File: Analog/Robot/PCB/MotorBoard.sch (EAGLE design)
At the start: 12 parts, among them U1 MSP430G2X53_20P

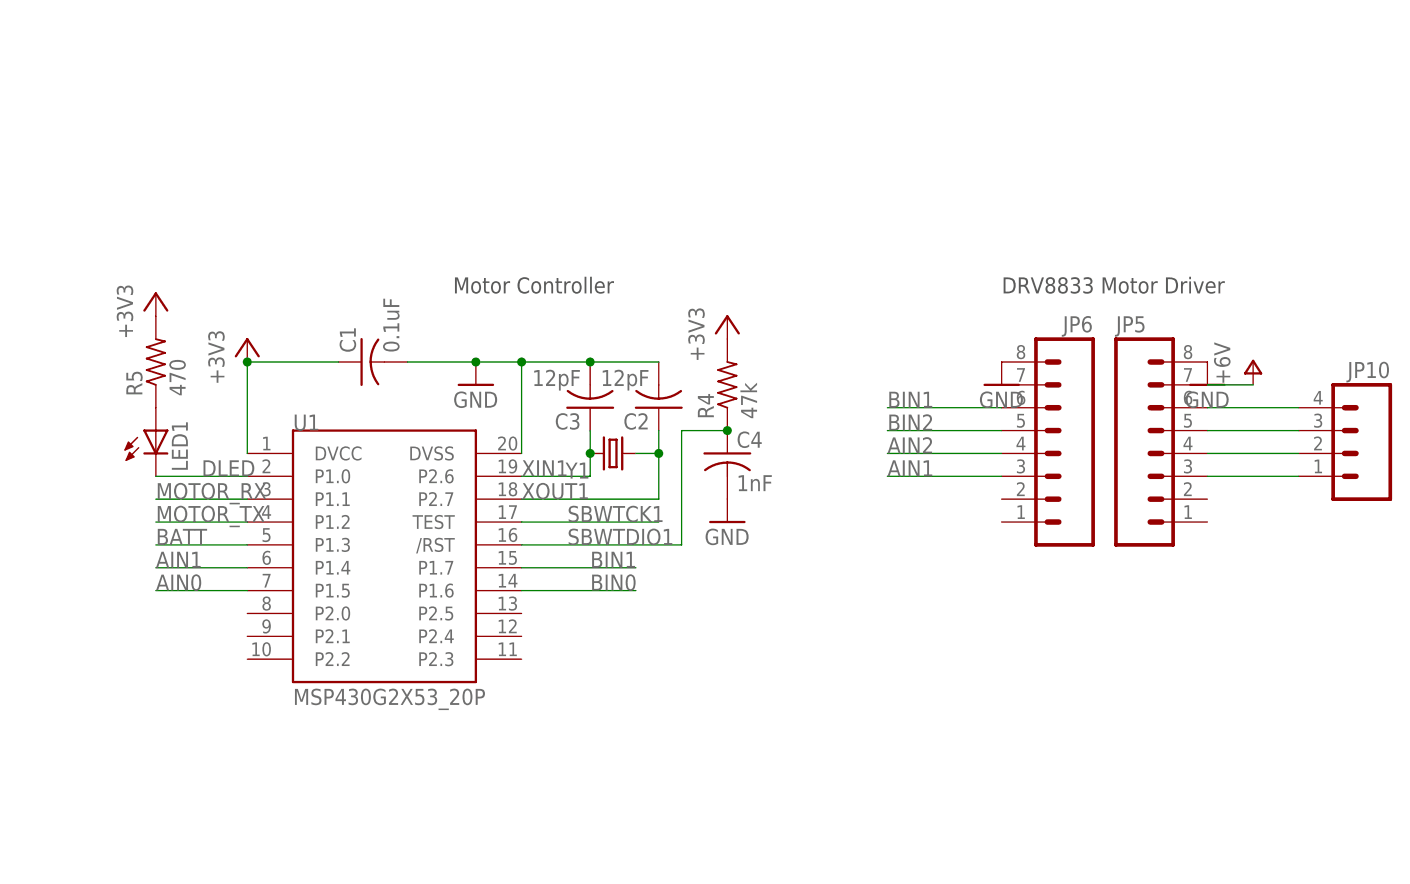
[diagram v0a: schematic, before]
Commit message: Board final; SPI progress
Sent PCBs to FAB
SPI driver working for multi-byte.  Bug: bytes are sent in reversed
order, although bit ordering (MSB first) is correct.
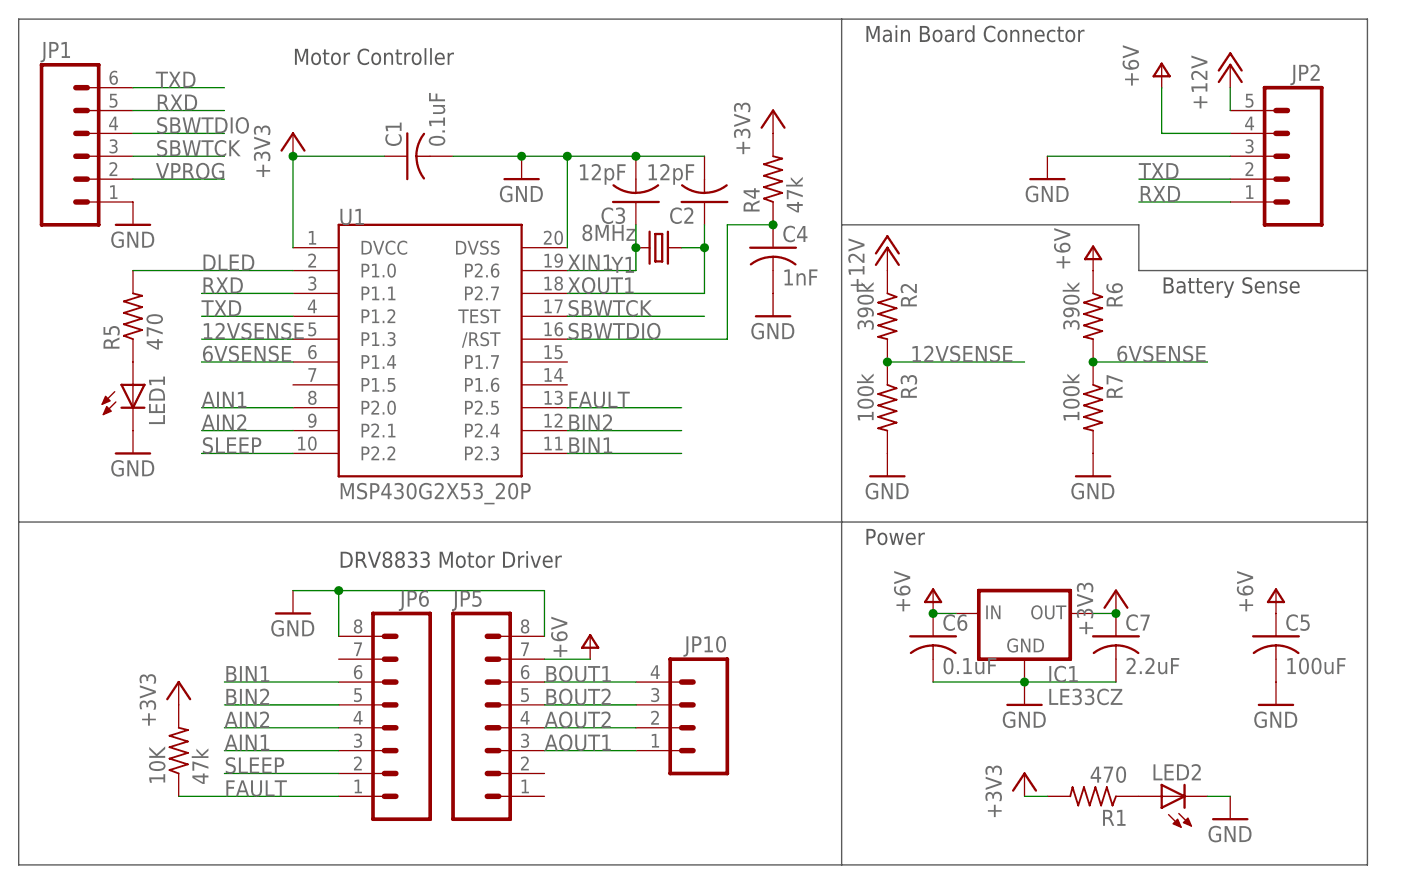
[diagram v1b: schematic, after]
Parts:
- added 10K: 47k, rcl:R-US_R0805
- added C5: 100uF, rcl:C-USC0805
- added C6: 0.1uF, rcl:C-USC0805
- added C7: 2.2uF, rcl:C-USC0805
- added IC1: LE33CZ, SparkFun-PowerIC:V_REG_78XXTO-92
- added JP1: (no value), SparkFun-Connectors:M06SIP
- added JP2: (no value), SparkFun-Connectors:M05PTH
- added LED2: (no value), led:LEDCHIP-LED0805
- added R1: 470, rcl:R-US_R0805
- added R2, R6: 390k, rcl:R-US_R0805
- added R3, R7: 100k, rcl:R-US_R0805
- Y1: value (none) -> 8MHz
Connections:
- net N$23 renamed AOUT1
- net N$24 renamed AOUT2
- net N$25 renamed BOUT2
- net N$30 renamed BOUT1
- removed net AIN0: U1.P1.5
- removed net BATT: U1.P1.3
- removed net BIN0: U1.P1.6
- removed net MOTOR_RX: U1.P1.1
- removed net MOTOR_TX: U1.P1.2
- removed net SBWTCK1: U1.TEST
- removed net SBWTDIO1: C4.1, R4.1, U1./RST
- new net +12V: JP2.5, R2.1
- new net 12VSENSE: R2.2, R3.1, U1.P1.3
- new net 6VSENSE: R6.2, R7.1, U1.P1.4
- new net FAULT: 10K.1, JP6.1, U1.P2.5
- new net N$5: LED2.A, R1.1
- new net RXD: JP1.5, JP2.1, U1.P1.1
- new net SBWTCK: JP1.3, U1.TEST
- new net SBWTDIO: C4.1, JP1.4, R4.1, U1./RST
- new net SLEEP: JP6.2, U1.P2.2
- new net TXD: JP1.6, JP2.2, U1.P1.2
- new net VPROG: JP1.2
- net +3V3: now also 10K.2, C7.1, IC1.OUT, R1.2; no longer R5.2
- net AIN1: now also U1.P2.0; no longer U1.P1.4
- net AIN2: now also U1.P2.1
- net BIN1: now also U1.P2.3; no longer U1.P1.7
- net BIN2: now also U1.P2.4
- net DLED: now also R5.2; no longer LED1.C
- net GND: now also C5.2, C6.2, C7.2, IC1.GND, JP1.1, JP2.3, LED1.C, LED2.C, R3.2, R7.2
- net V+: now also C5.1, C6.1, IC1.IN, JP2.4, R6.1
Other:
- note added: "Battery Sense"
- note added: "Main Board Connector"
- note added: "Power"
- moved on the sheet: C1, C2, C3, C4, JP10, JP5, JP6, LED1, R4, R5, U1, Y1
